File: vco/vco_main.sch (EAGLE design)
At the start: 101 parts, among them IC1 OPA4130U, IC2 LM13700M, IC3 OPA4130U, IC4 OPA4130U, Q1 MMBFJ3

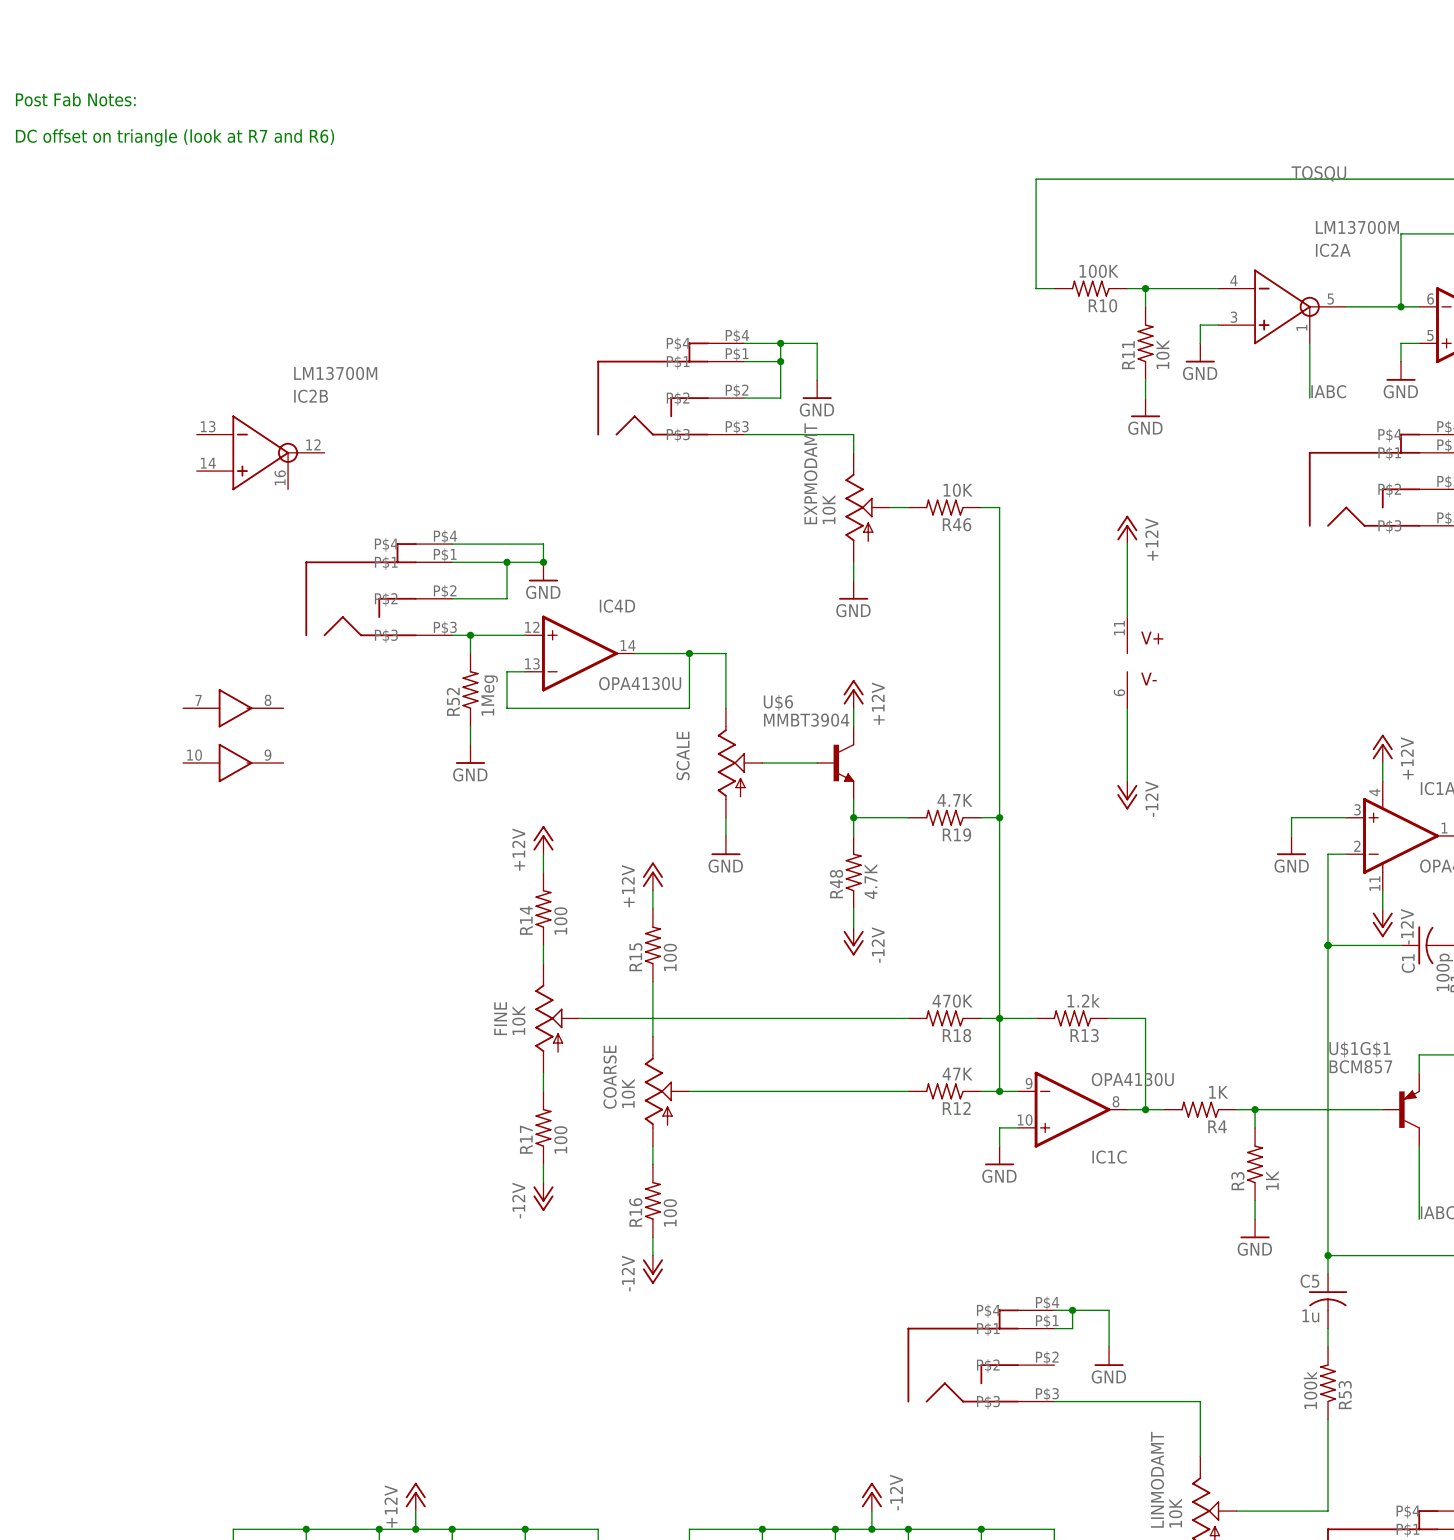
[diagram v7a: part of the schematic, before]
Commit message: made some small changes that drove me crazy during assembly.
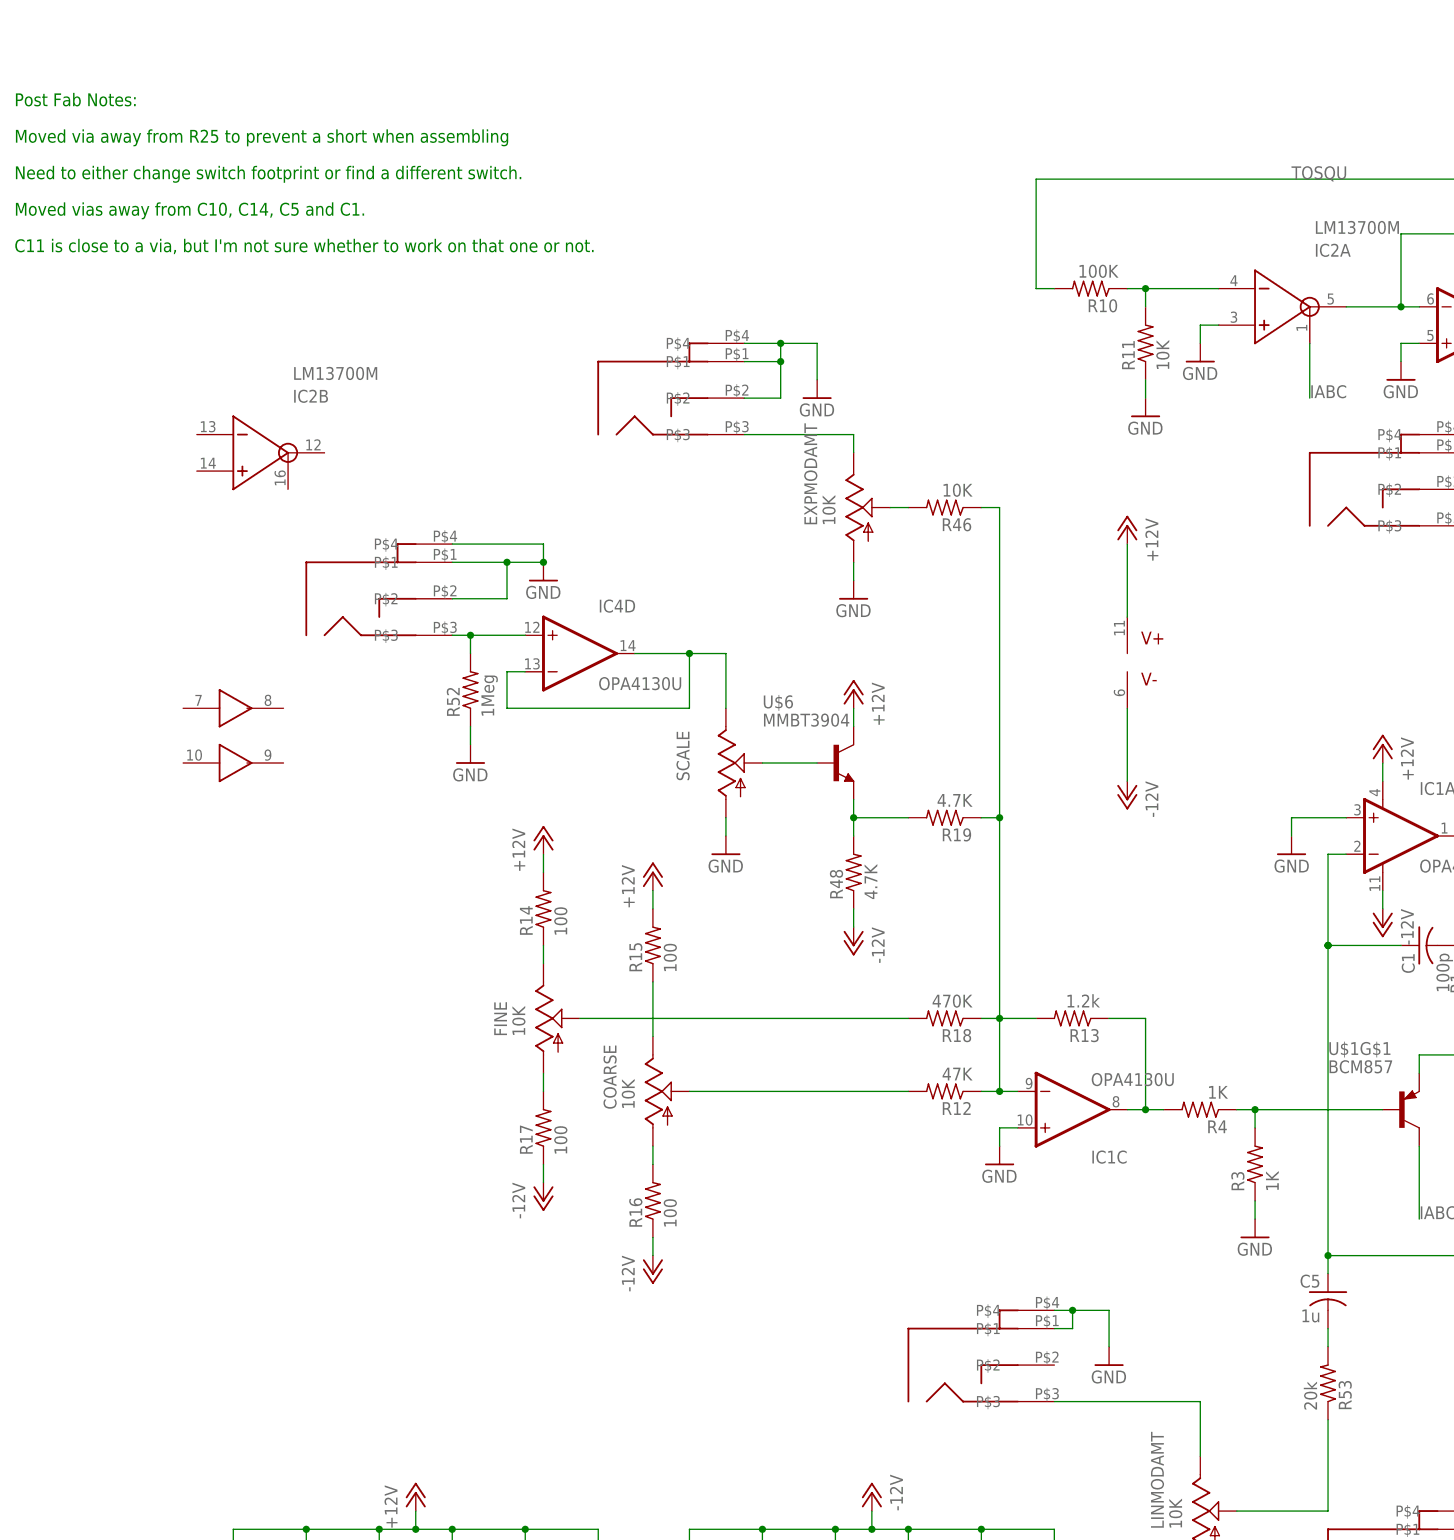
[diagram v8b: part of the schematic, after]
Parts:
- R53: value 100k -> 20k
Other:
- note added: "C11 is close to a via, but I'm not sure whether to work on that one or not."
- note added: "Moved via away from R25 to prevent a short when assembling"
- note added: "Moved vias away from C10, C14, C5 and C1."
- note added: "Need to either change switch footprint or find a different switch."
- note removed: "DC offset on triangle (look at R7 and R6)"
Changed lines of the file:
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@@
 <part name="GND37" library="dan" deviceset="GND" device=""/>
 <part name="GND38" library="dan" deviceset="GND" device=""/>
-<part name="R53" library="dan" deviceset="R-US_" device="R0603" value="100k"/>
+<part name="R53" library="dan" deviceset="R-US_" device="R0603" value="20k"/>
 <part name="LED1" library="dan" deviceset="LED" device="5MM"/>
 </parts>
@@
 <text x="165.1" y="132.08" size="1.778" layer="91">Verify location of sync input</text>
 <text x="-121.92" y="154.94" size="1.778" layer="91">Post Fab Notes:</text>
-<text x="-121.92" y="149.86" size="1.778" layer="91">DC offset on triangle (look at R7 and R6)</text>
+<text x="-121.92" y="149.86" size="1.778" layer="91">Moved via away from R25 to prevent a short when assembling</text>
+<text x="-121.92" y="144.78" size="1.778" layer="91">Need to either change switch footprint or find a different switch.</text>
+<text x="-121.92" y="139.7" size="1.778" layer="91">Moved vias away from C10, C14, C5 and C1.</text>
+<text x="-121.92" y="134.62" size="1.778" layer="91">C11 is close to a via, but I'm not sure whether to work on that one or not.</text>
 </plain>
 <instances>
